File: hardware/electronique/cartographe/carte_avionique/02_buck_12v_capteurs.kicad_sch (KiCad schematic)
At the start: 10 parts, among them J201 SORTIE 12V_LIDAR, U201 LM76003 / 12V_LIDAR

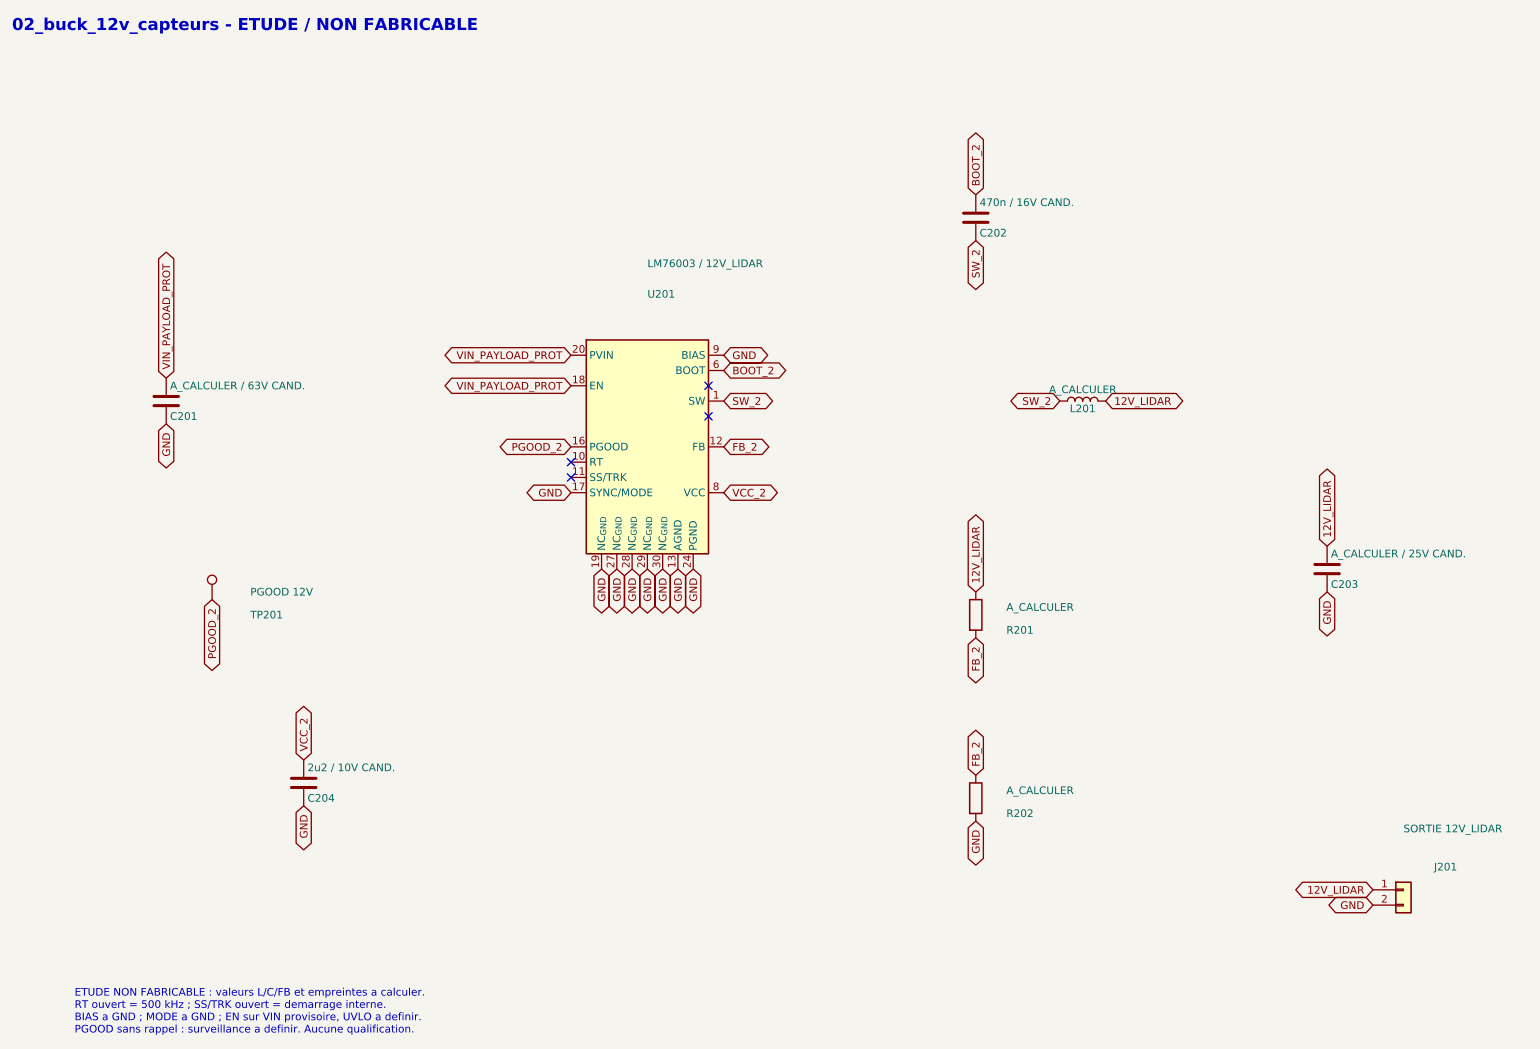
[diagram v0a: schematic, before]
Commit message: feat(hw): compléter CA01 et clarifier la synchronisation des captures
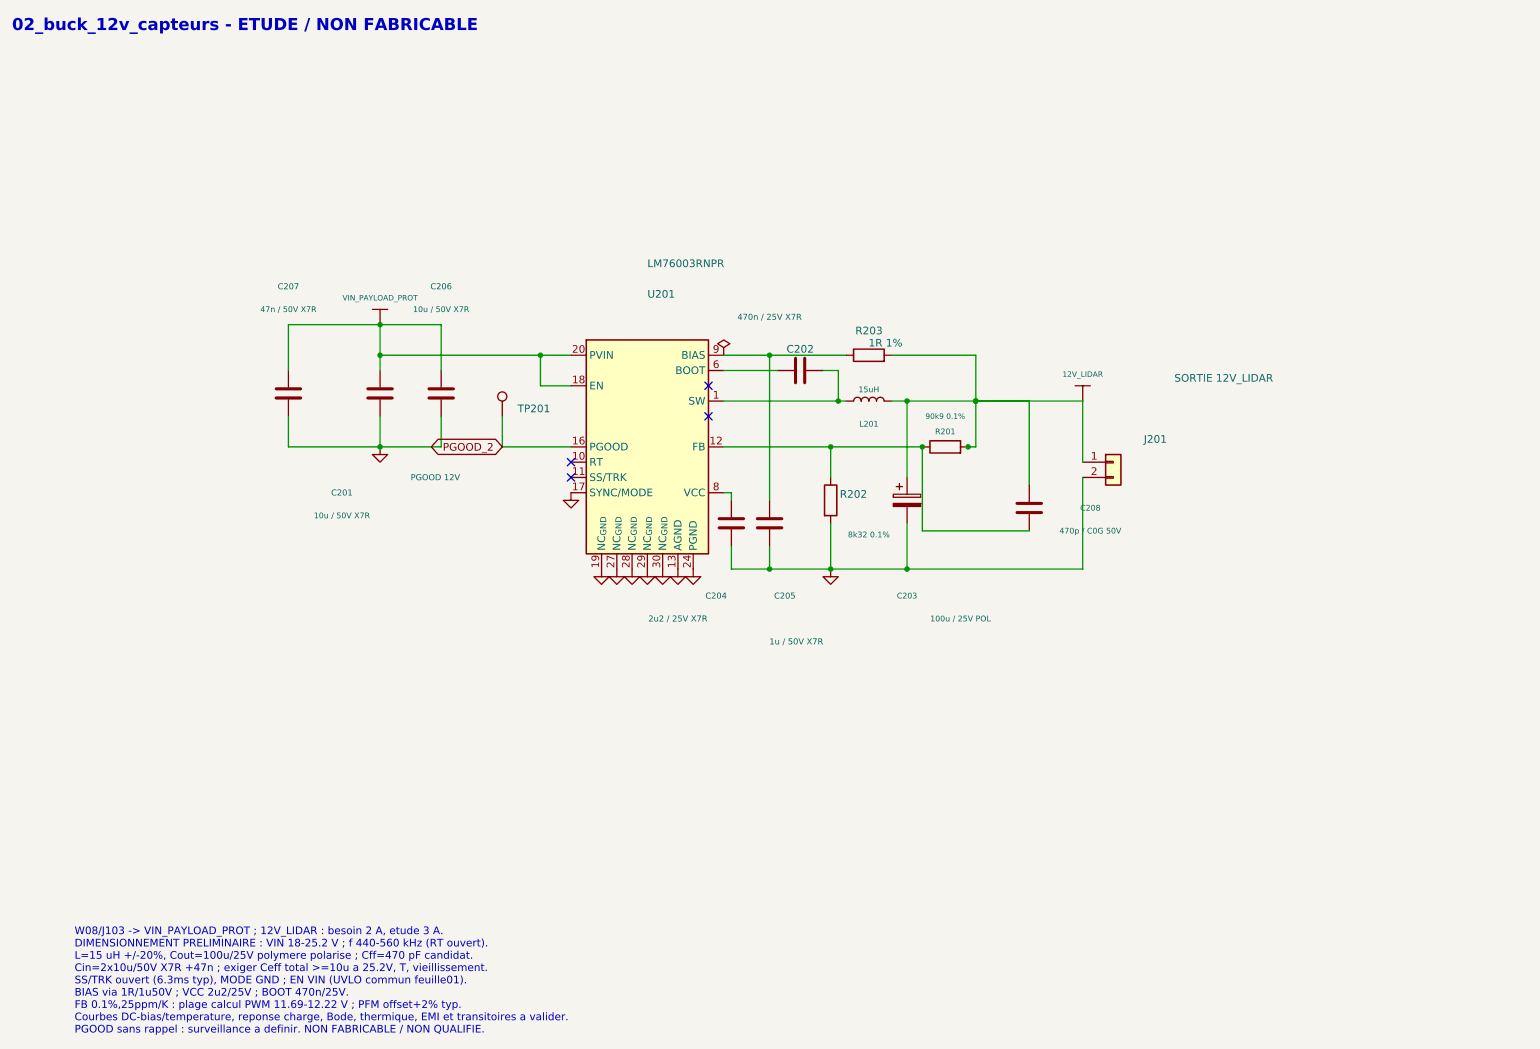
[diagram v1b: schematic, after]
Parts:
- added C205: 1u / 50V X7R, Capacitor_SMD:C_0603_1608Metric, symbol Device:C
- added C206: 10u / 50V X7R, Capacitor_SMD:C_1210_3225Metric, symbol Device:C
- added C207: 47n / 50V X7R, Capacitor_SMD:C_0603_1608Metric, symbol Device:C
- added C208: 470p / C0G 50V, Capacitor_SMD:C_0603_1608Metric, symbol Device:C
- added R203: 1R 1%, Resistor_SMD:R_0603_1608Metric, symbol Device:R
- C201: value A_CALCULER / 63V CAND. -> 10u / 50V X7R; footprint (none) -> Capacitor_SMD:C_1210_3225Metric; Design_status (none) -> A valider - calcul preliminaire 2026-09-29; MPN (none) -> C3225X7R1H106K250AC; Manufacturer (none) -> TDK
- C202: value 470n / 16V CAND. -> 470n / 25V X7R; footprint (none) -> Capacitor_SMD:C_0603_1608Metric; Design_status (none) -> A valider - calcul preliminaire 2026-09-29; MPN (none) -> C1608X7R1E474K080AB; Manufacturer (none) -> TDK
- C203: value A_CALCULER / 25V CAND. -> 100u / 25V POL; footprint (none) -> Capacitor_SMD:CP_Elec_8x6.9; symbol Device:C -> Device:C_Polarized; Design_status (none) -> A valider - calcul preliminaire 2026-09-29; MPN (none) -> 25SVPF100M; Manufacturer (none) -> Panasonic
- C204: value 2u2 / 10V CAND. -> 2u2 / 25V X7R; footprint (none) -> Capacitor_SMD:C_0805_2012Metric; Design_status (none) -> A valider - calcul preliminaire 2026-09-29; MPN (none) -> C2012X7R1E225K125AB; Manufacturer (none) -> TDK
- L201: value A_CALCULER -> 15uH; footprint (none) -> Inductor_SMD:L_Coilcraft_XAL1010-XXX; Design_status (none) -> A valider - calcul preliminaire 2026-09-29; MPN (none) -> XAL1010-153MED; Manufacturer (none) -> Coilcraft
- R201: value A_CALCULER -> 90k9 0.1%; footprint (none) -> Resistor_SMD:R_0603_1608Metric; Design_status (none) -> A valider - calcul preliminaire 2026-09-29; MPN (none) -> TNPW060390K9BEEA; Manufacturer (none) -> Vishay
- R202: value A_CALCULER -> 8k32 0.1%; footprint (none) -> Resistor_SMD:R_0603_1608Metric; Design_status (none) -> A valider - calcul preliminaire 2026-09-29; MPN (none) -> TNPW06038K32BEEA; Manufacturer (none) -> Vishay
- U201: value LM76003 / 12V_LIDAR -> LM76003RNPR; Design_status (none) -> A valider - calcul preliminaire 2026-09-29; MPN (none) -> LM76003RNPR; Manufacturer (none) -> Texas Instruments
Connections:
- net 12V_LIDAR: now also R201.2, C208.1, R203.2; no longer R201.1
- net GND: now also C205.2, C206.2, C207.2; no longer U201.9 (BIAS)
- net VIN_PAYLOAD_PROT: now also C206.1, C207.1
- net BOOT_2: no longer names the net of C202.1, U201.6 (BOOT)
- net FB_2: no longer names the net of R202.1, U201.12 (FB)
- net FB_2: now also R201.1, C208.2; no longer R201.2
- net SW_2: no longer names the net of C202.2, L201.1, U201.1 (SW), U201.2 (SW), U201.3 (SW), U201.4 (SW), U201.5 (SW)
- net VCC_2: no longer names the net of C204.1, U201.8 (VCC)
- new net: C205.1, R203.1, U201.9 (BIAS)
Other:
- note added: "W08/J103 -> VIN_PAYLOAD_PROT ; 12V_LIDAR : besoin 2 A, etude 3 A. DIMENSIONNEMENT PRELIMINAIRE : VIN 18-25.2 V ; f 440-560 kHz (RT ouvert). L=15 uH +/-20%, Cout=100u/25V polymere polarise ; Cff=470 pF candidat. Cin=2x10u/50V X7R +47n ; exiger Ceff total >=10u a 25.2V, T, vieillissement. SS/TRK ouvert (6.3ms typ), MODE GND ; EN VIN (UVLO commun feuille01). BIAS via 1R/1u50V ; VCC 2u2/25V ; BOOT 47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"
- note removed: "ETUDE NON FABRICABLE : valeurs L/C/FB et empreintes a calculer. RT ouvert = 500 kHz ; SS/TRK ouvert = demarrage interne. BIAS a GND ; MODE a GND ; EN sur VIN provisoire, UVLO a definir. PGOOD sans rappel : surveillance a definir. Aucune qualification."
- moved on the sheet: C201, C202, C204, J201, L201, R201, R202, TP201
